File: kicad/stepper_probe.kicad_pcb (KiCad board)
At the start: 2 copper layers, 33 x 42 mm, 50 parts, among them J1 Conn_01x04_Male, J2 Conn_01x04_Male, J3 BAT, J4 Conn_01x03_Male, J5 SWD, J6 Reset header, M1 Motor, Q1 PJA3439, SW1 SW_Push, U1 CC6920BSO-5A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

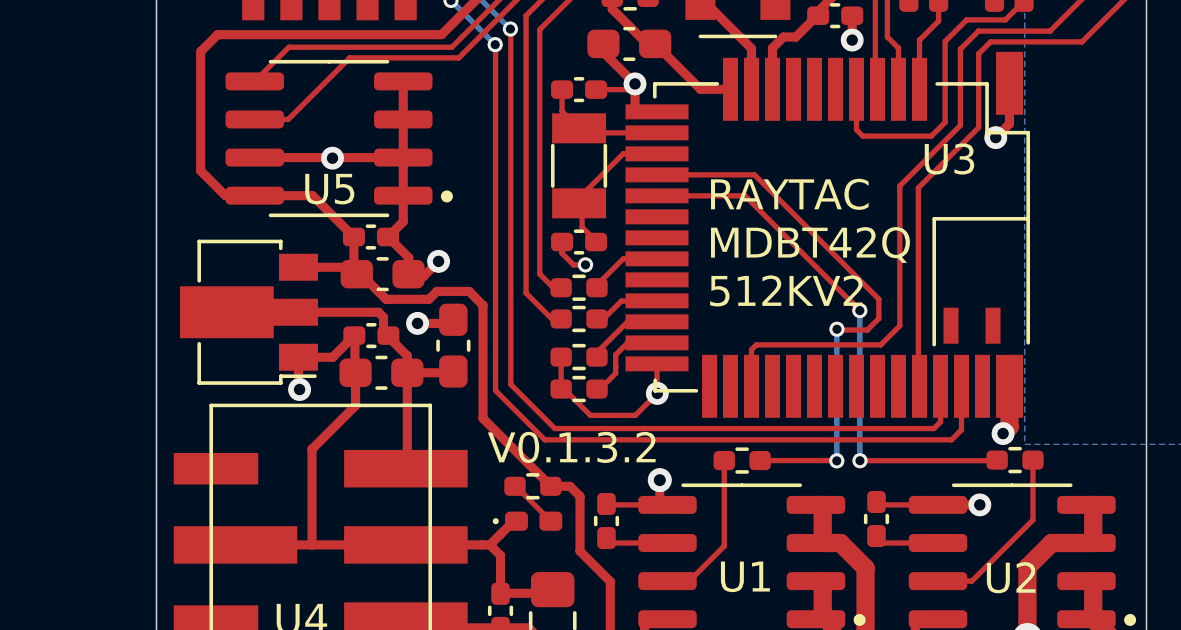
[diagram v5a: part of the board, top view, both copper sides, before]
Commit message: Cleaned up kicad 6 files.
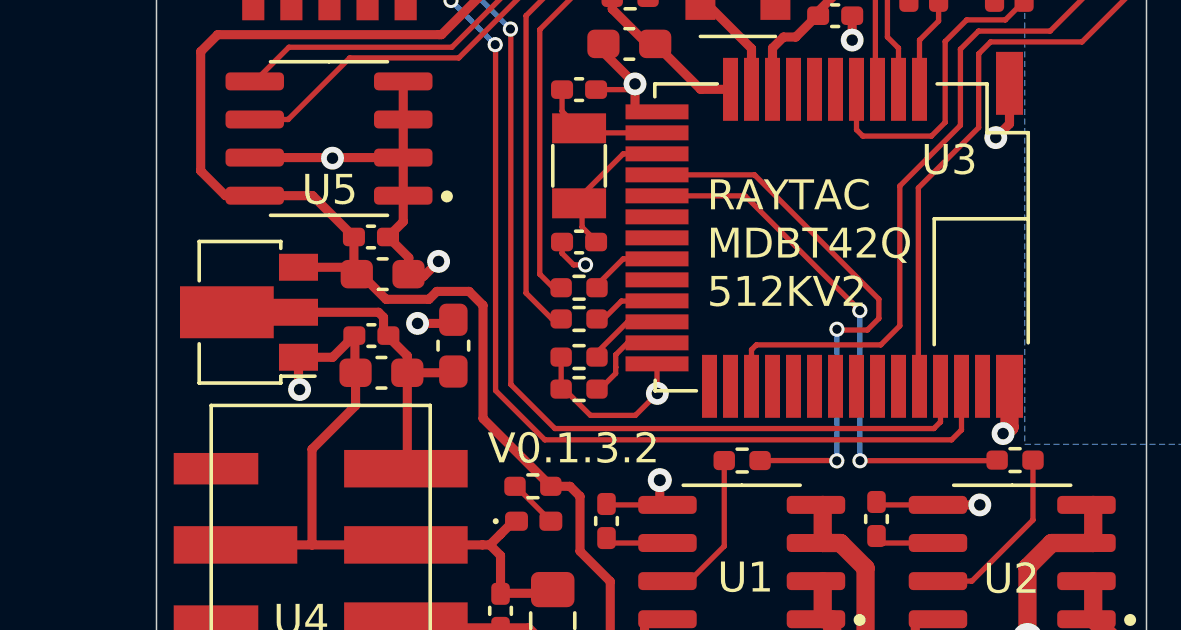
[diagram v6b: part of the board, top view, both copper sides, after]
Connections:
- J5 pad 10: Net-(J5-Pad10) -> unconnected-(J5-Pad10)
- J5 pad 6: Net-(J5-Pad6) -> unconnected-(J5-Pad6)
- J5 pad 7: Net-(J5-Pad7) -> unconnected-(J5-Pad7)
- J5 pad 8: Net-(J5-Pad8) -> unconnected-(J5-Pad8)
- U3 pad 17: Net-(U3-Pad17) -> unconnected-(U3-Pad17)
- U3 pad 18: Net-(U3-Pad18) -> unconnected-(U3-Pad18)
- U3 pad 20: Net-(U3-Pad20) -> unconnected-(U3-Pad20)
- U3 pad 25: /TEST1 -> unconnected-(U3-Pad25)
- U3 pad 26: /TEST2 -> unconnected-(U3-Pad26)
- U3 pad 28: Net-(U3-Pad28) -> unconnected-(U3-Pad28)
- U3 pad 29: Net-(U3-Pad29) -> unconnected-(U3-Pad29)
- U3 pad 30: Net-(U3-Pad30) -> unconnected-(U3-Pad30)
- U3 pad 31: Net-(U3-Pad31) -> unconnected-(U3-Pad31)
- U3 pad 32: Net-(U3-Pad32) -> unconnected-(U3-Pad32)
- U3 pad 33: Net-(U3-Pad33) -> unconnected-(U3-Pad33)
- U3 pad 34: Net-(U3-Pad34) -> unconnected-(U3-Pad34)
- U3 pad 38: Net-(U3-Pad38) -> unconnected-(U3-Pad38)
- U3 pad 6: Net-(U3-Pad6) -> unconnected-(U3-Pad6)
- U3 pad 7: Net-(U3-Pad7) -> unconnected-(U3-Pad7)
- U3 pad 8: Net-(U3-Pad8) -> unconnected-(U3-Pad8)
- U4 pad 4: (no net) -> unconnected-(U4-Pad4)
- U4 pad 6: (no net) -> unconnected-(U4-Pad6)
